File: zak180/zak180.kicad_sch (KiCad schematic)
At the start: 1 part, among them U39 74HC04

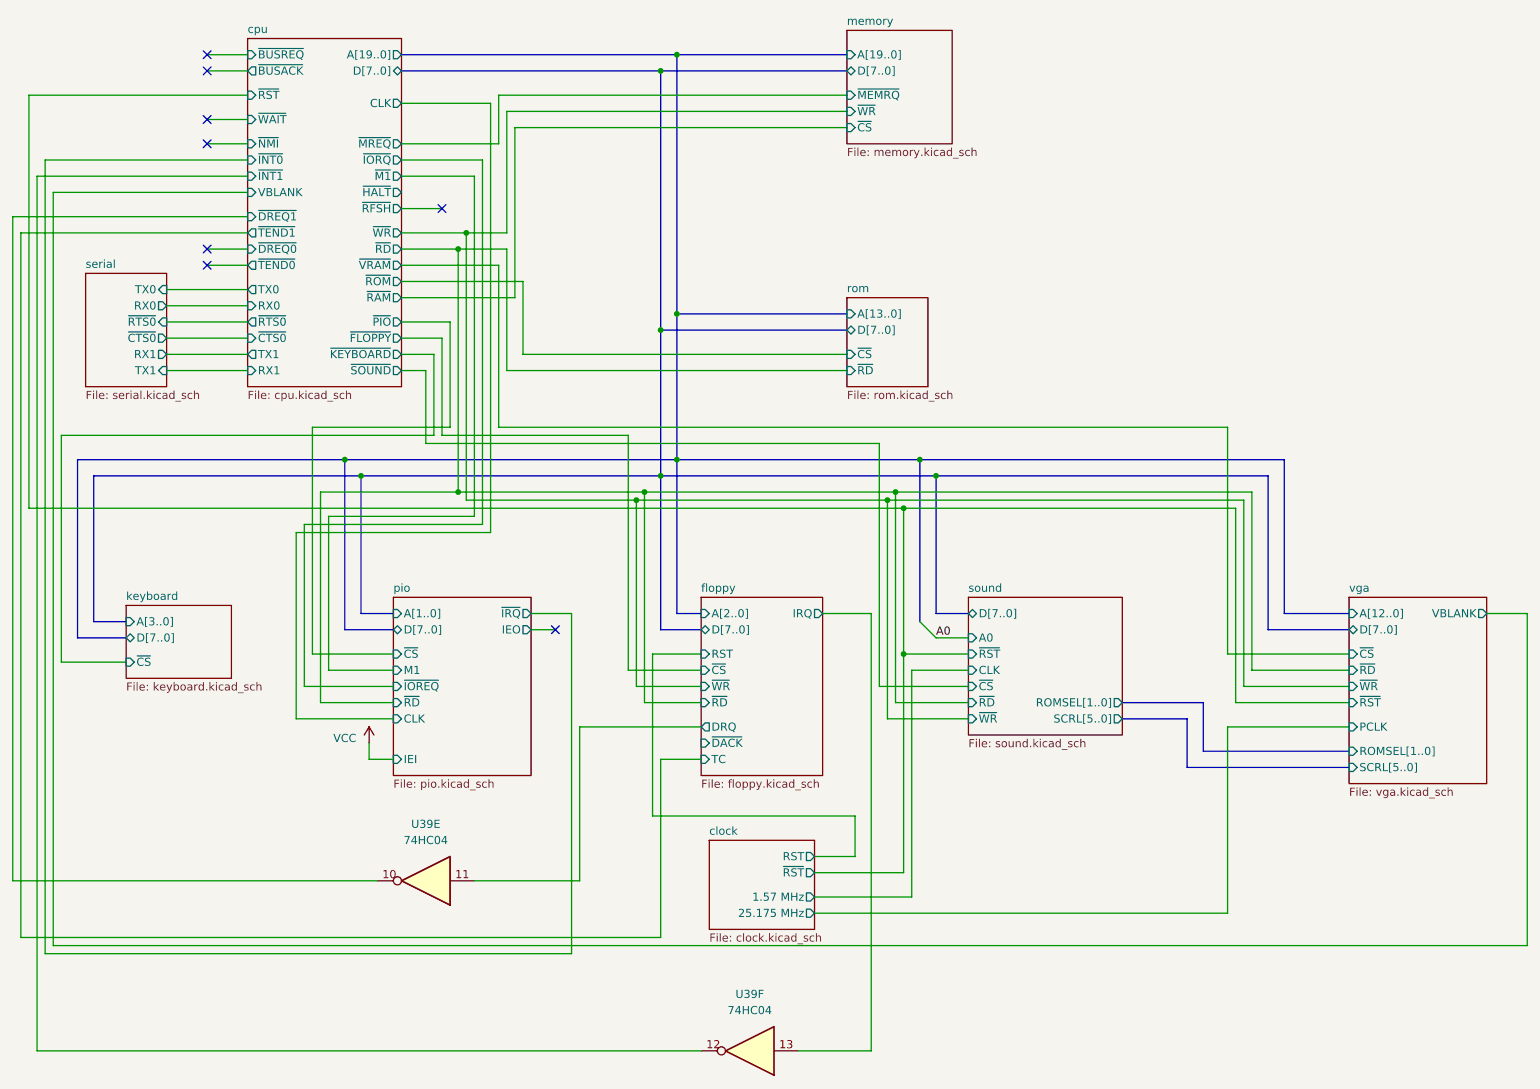
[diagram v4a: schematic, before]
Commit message: HW: Change RAM to static
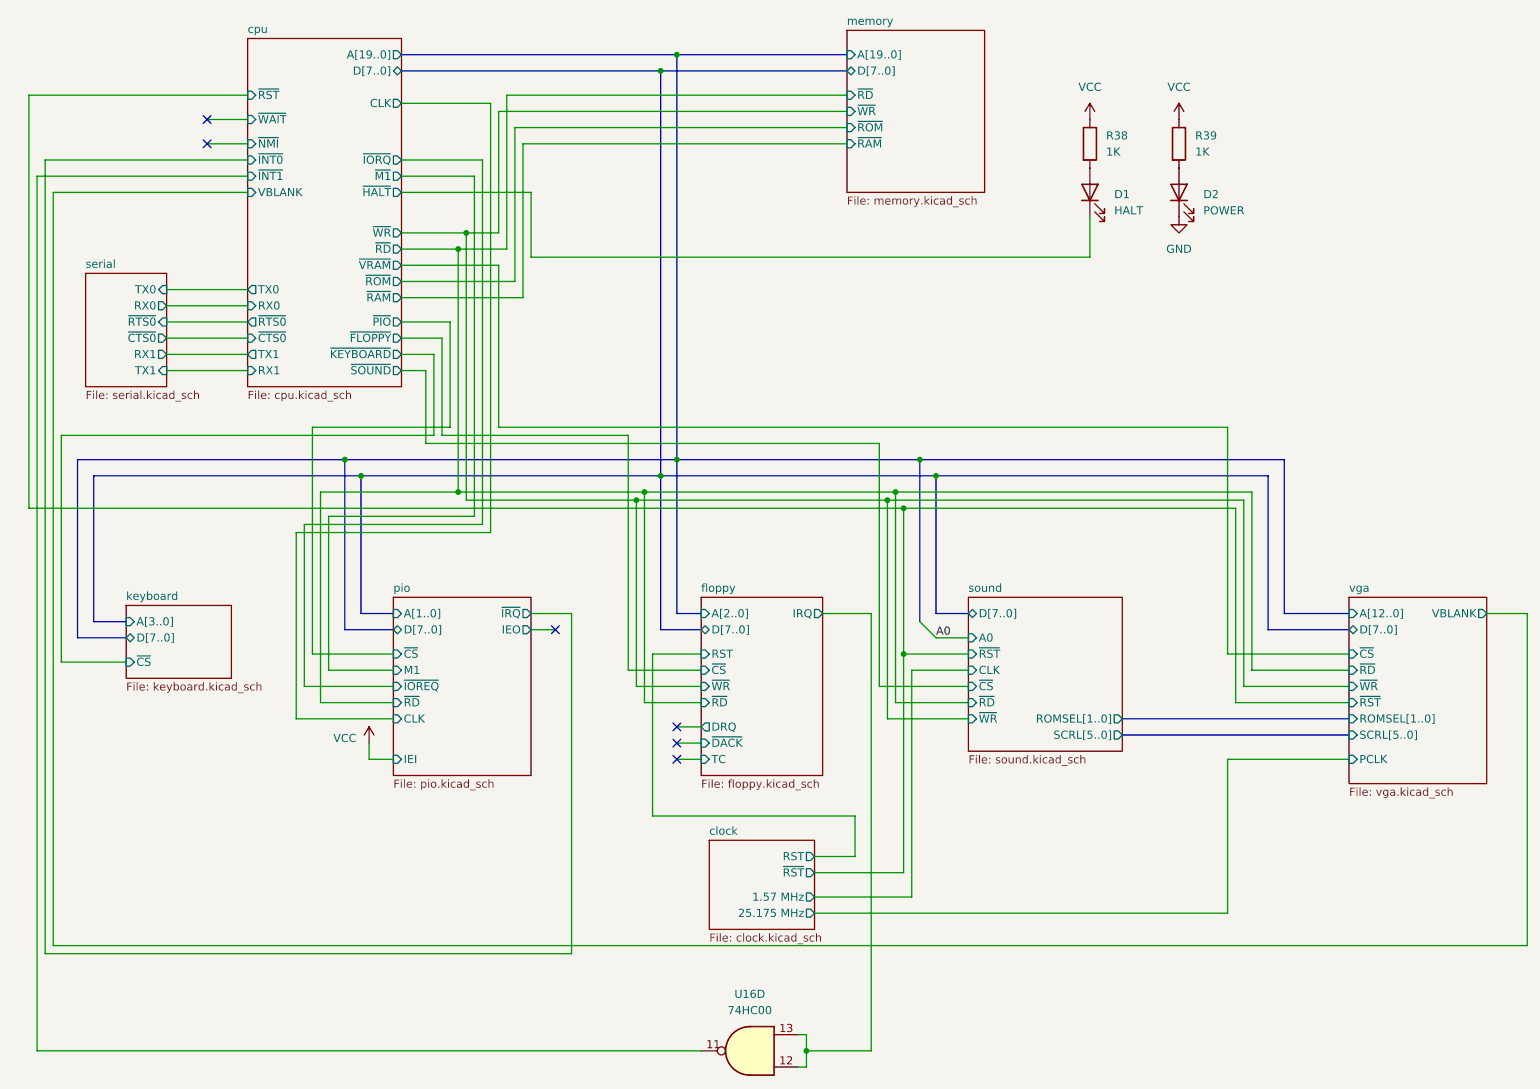
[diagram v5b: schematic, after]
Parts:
- removed U39: 74HC04, symbol 74xx:74HC04
- added D1: HALT, LED_THT:LED_D5.0mm, symbol Device:LED
- added D2: POWER, LED_THT:LED_D5.0mm, symbol Device:LED
- added R38, R39: 1K, Resistor_THT:R_Axial_DIN0207_L6.3mm_D2.5mm_P7.62mm_Horizontal, symbol Device:R
- added U16: 74HC00, Package_DIP:DIP-14_W7.62mm, symbol 74xx:74HC00
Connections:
- net VCC: now also R38.1, R39.1
- net cpu/~{HALT}: now also D1.1 (K)
- net cpu/~{INT1}: now also U16.11
- net floppy/IRQ: now also U16.12, U16.13
- new net: D1.2 (A), R38.2
- new net: D2.2 (A), R39.2
- new net GND: D2.1 (K)
- no-connect marks 8 -> 6
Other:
- removed sheet rom
- sheet cpu ports: added none; removed ~{BUSACK}, ~{BUSREQ}, ~{DREQ0}, ~{DREQ1}, ~{MREQ}, ~{RFSH}, ~{TEND0}, ~{TEND1}
- sheet memory ports: added ~{RAM}, ~{RD}, ~{ROM}; removed ~{CS}, ~{MEMRQ}
